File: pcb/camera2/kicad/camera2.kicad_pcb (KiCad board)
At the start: 4 copper layers, 96.5 x 45.7 mm, 56 parts

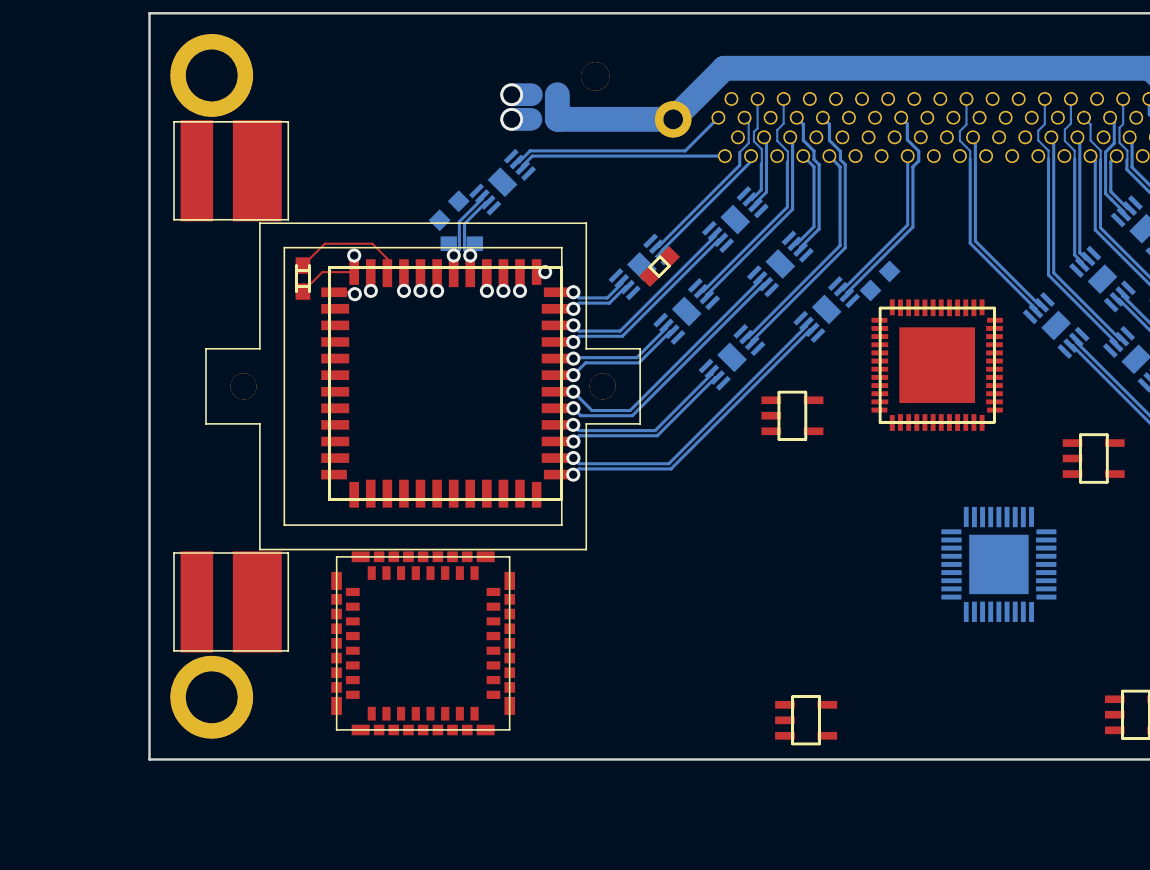
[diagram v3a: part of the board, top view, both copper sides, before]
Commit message: external CPLD pins routed
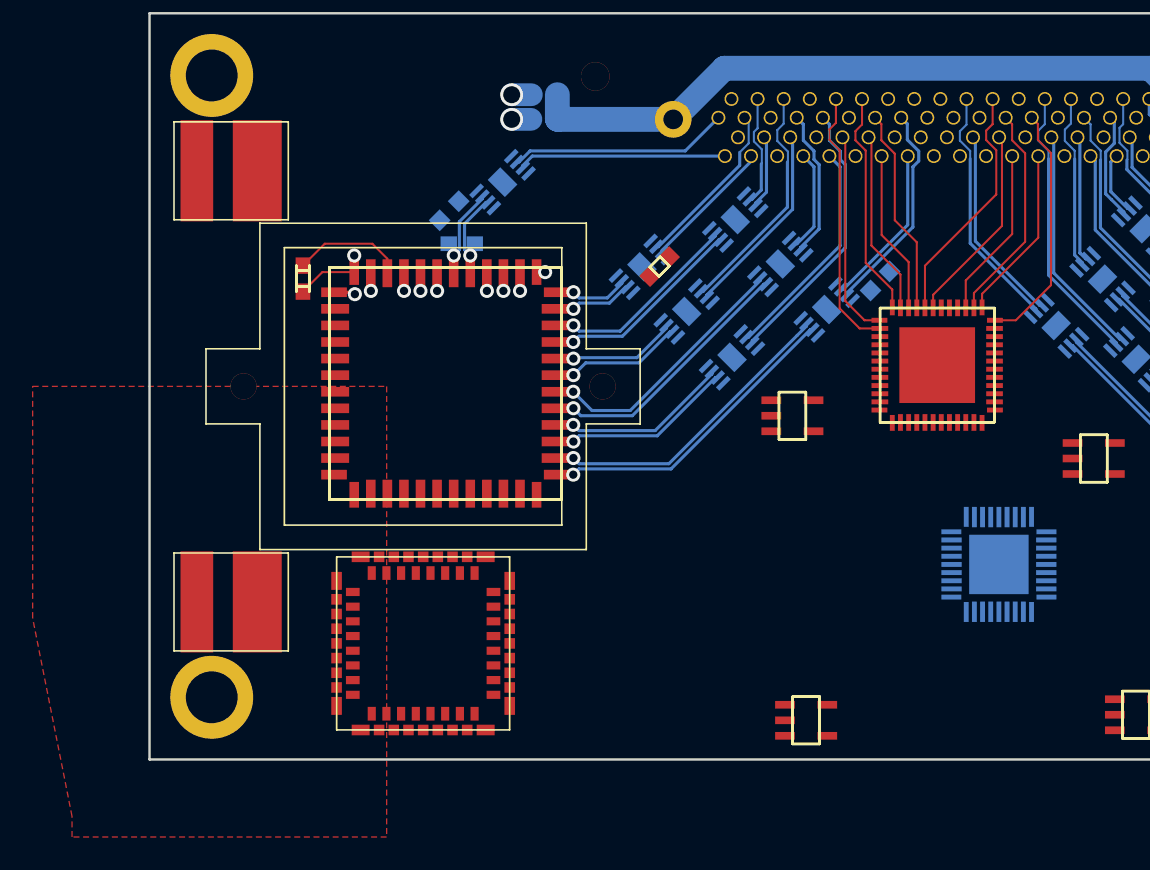
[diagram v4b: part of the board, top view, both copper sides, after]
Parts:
- B1, B10, B11, B15, B16, B17, B18, B19, B2, B20, B3, B4, B5, B6: footprint gen:b84940fdfb16a2d7942b3b406dd98b10c2c2213999c6866e353299b244b8fc6e -> gen:cbfca23ea51b44d0e50a3924c338fdaf501ecf837853ca0935bf710595246917
- C1U1, C2U1: footprint gen:c58747e0684f9d36f894e920eb782c552f159bd2e92cf7dd16541e289be4d654 -> gen:29d36b60264305e3bb3ff8193f908c1e023f0724867315a44096beda3859eb57
- REG0: footprint gen:a8a9fe32768e32ddc75aa8295cef6929db764d9ac77e4627a54db0fef3c1f31a -> gen:ed70987c828567e2e09b177ee862bde5f7a38a9fe78d493e29e57c7e20deaf47
- REG1: footprint gen:0ebfd6ab58889eb03d8f26c7dd1b53306c9215b0059415f86bfdbb9abe3fdde1 -> gen:2bd25f7f1c5714eb7bf2f04a481733791fc5506059f66161b644c94ef96df4e5
- REG2: footprint gen:eb209b2e1d221af71ed48e28bfe0bb8298d616a411442e29f3453ccc73495e89 -> gen:97f27c9ee76a9ddcafed8a13eebe55523c4eda27fc57fcfd9b753b732235d5a3
- REG3: footprint gen:5bda942c242ea2bebc3cf29ef5f6c3ab9ee59d551a6204d93c9eca0998310be8 -> gen:115de365bb93de9cdb0d1863ddce6b36c3ff55cc7ac346e1776ef7a0d0952155
- U1: footprint gen:2f9b442f54b7add4956d34ec651f64beab61546dadc67e38d2c3fc0b09ac9096 -> gen:f8d22c0c24f01065a72fabcbb4d2d21d35812c608890a960801174ad3b2e1a64
- U2: footprint gen:cf96d1af73b58f8f1f3d64f5194d5234fe541250e2558da2cd5d85457dfd18e6 -> gen:230388a9e77c447920cc8d9b60ac5542707622b54124d58dc54acd5e8b04156f
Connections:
- net B10_1 renamed B10_1_NC
- net B10_4 renamed B10_4_NC
- net B10_5 renamed B10_5_NC
- net B11_1 renamed B11_1_NC
- net B11_4 renamed B11_4_NC
- net B11_5 renamed B11_5_NC
- net B15_1 renamed B15_1_NC
- net B15_4 renamed B15_4_NC
- net B15_5 renamed B15_5_NC
- net B16_1 renamed B16_1_NC
- net B16_4 renamed B16_4_NC
- net B16_5 renamed B16_5_NC
- net B17_1 renamed B17_1_NC
- net B17_4 renamed B17_4_NC
- net B17_5 renamed B17_5_NC
- net B18_1 renamed B18_1_NC
- net B18_4 renamed B18_4_NC
- net B18_5 renamed B18_5_NC
- net B19_1 renamed B19_1_NC
- net B19_4 renamed B19_4_NC
- net B19_5 renamed B19_5_NC
- net B1_1 renamed B1_1_NC
- net B1_4 renamed B1_4_NC
- net B1_5 renamed B1_5_NC
- net B20_1 renamed B20_1_NC
- net B20_4 renamed B20_4_NC
- net B20_5 renamed B20_5_NC
- net B2_1 renamed B2_1_NC
- net B2_4 renamed B2_4_NC
- net B2_5 renamed B2_5_NC
- net B3_1 renamed B3_1_NC
- net B3_4 renamed B3_4_NC
- net B3_5 renamed B3_5_NC
- net B4_1 renamed B4_1_NC
- net B4_4 renamed B4_4_NC
- net B4_5 renamed B4_5_NC
- net B5_1 renamed B5_1_NC
- net B5_4 renamed B5_4_NC
- net B5_5 renamed B5_5_NC
- net B6_1 renamed B6_1_NC
- net B6_4 renamed B6_4_NC
- net B6_5 renamed B6_5_NC
- net D0_1 renamed D0_1_C
- net D0_2 renamed D0_2_A
- net D1_1 renamed D1_1_C
- net D1_2 renamed D1_2_A
- net D2_1 renamed D2_1_C
- net D2_2 renamed D2_2_A
- net D3_1 renamed D3_1_C
- net D3_2 renamed D3_2_A
- net REG0_4 renamed REG0_4_NC
- net REG1_4 renamed REG1_4_NC
- net REG2_4 renamed REG2_4_NC
- net REG3_4 renamed REG3_4_NC
- net T1_17 renamed T1_17_NC
- net T1_2 renamed T1_2_GPIO3
- net T1_23 renamed T1_23_PWR_DWN_L
- net T1_24 renamed T1_24_RESET_L
- net T1_26 renamed T1_26_MASTER_CLK
- net T1_28 renamed T1_28_MIPI_CLK_N
- net T1_29 renamed T1_29_MIPI_CLK_P
- net T1_3 renamed T1_3_GPIO2
- net T1_31 renamed T1_31_MIPI_DATA_N
- net T1_32 renamed T1_32_MIPI_DATA_P
- net T1_4 renamed T1_4_GPIO1
- net T1_5 renamed T1_5_GPIO0
- net T2_17 renamed T2_17_NC
- net T2_2 renamed T2_2_GPIO3
- net T2_23 renamed T2_23_PWR_DWN_L
- net T2_24 renamed T2_24_RESET_L
- net T2_26 renamed T2_26_MASTER_CLK
- net T2_28 renamed T2_28_MIPI_CLK_N
- net T2_29 renamed T2_29_MIPI_CLK_P
- net T2_3 renamed T2_3_GPIO2
- net T2_31 renamed T2_31_MIPI_DATA_N
- net T2_32 renamed T2_32_MIPI_DATA_P
- net T2_4 renamed T2_4_GPIO1
- net T2_5 renamed T2_5_GPIO0
- net U1_10 renamed U1_10_PA3
- net U1_11 renamed U1_11_PA4
- net U1_12 renamed U1_12_PA5
- net U1_13 renamed U1_13_PA6
- net U1_14 renamed U1_14_PA7
- net U1_15 renamed U1_15_PB0
- net U1_16 renamed U1_16_PB1
- net U1_17 renamed U1_17_PB2
- net U1_2 renamed U1_2_PD0
- net U1_20 renamed U1_20_PA8
- net U1_21 renamed U1_21_PA9
- net U1_22 renamed U1_22_PA10
- net U1_23 renamed U1_23_PA11
- net U1_24 renamed U1_24_PA12
- net U1_3 renamed U1_3_PD1
- net U1_32 renamed U1_32_PB5
- net U1_33 renamed U1_33_PB6
- net U1_34 renamed U1_34_PB7
- net U1_5 renamed U1_5_VSSA
- net U1_6 renamed U1_6_VDDA
- net U1_7 renamed U1_7_PA0
- net U1_8 renamed U1_8_PA1
- net U1_9 renamed U1_9_PA2
- net U2_10 renamed U2_10_IO1_10
- net U2_11 renamed U2_11_IO1_11
- net U2_12 renamed U2_12_IO1_12
- net U2_13 renamed U2_13_IO1_13
- net U2_14 renamed U2_14_IO1_14
- net U2_15 renamed U2_15_IO1_15
- net U2_17 renamed U2_17_IO1_17
- net U2_18 renamed U2_18_IO1_18
- net U2_20 renamed U2_20_IO1_20
- net U2_24 renamed U2_24_IO1_24
- net U2_25 renamed U2_25_IO1_25
- net U2_26 renamed U2_26_IO1_26
- net U2_27 renamed U2_27_IO1_27
- net U2_28 renamed U2_28_IO1_28
- net U2_30 renamed U2_30_IO1_30
- net U2_32 renamed U2_32_IO2_32
- net U2_33 renamed U2_33_IO2_33
- net U2_34 renamed U2_34_IO2_34
- net U2_35 renamed U2_35_IO2_35
- net U2_4 renamed U2_4_IO2_4
- net U2_5 renamed U2_5_IO2_5
- net U2_6 renamed U2_6_IO1_6
- net U2_7 renamed U2_7_IO1_7
- net U2_8 renamed U2_8_IO1_8
- net U2_9 renamed U2_9_IO1_9
- U2 pad 1: U2_1 -> pair7P
- U2 pad 2: U2_2 -> pair7N
- U2 pad 36: U2_36 -> pair14N
- U2 pad 37: U2_37 -> pair14P
- U2 pad 38: U2_38 -> pair13N
- U2 pad 39: U2_39 -> pair13P
- U2 pad 43: U2_43 -> pair12P
- U2 pad 44: U2_44 -> pair12N
- U2 pad 45: U2_45 -> pair9N
- U2 pad 46: U2_46 -> pair9P
- U2 pad 47: U2_47 -> pair8P
- U2 pad 48: U2_48 -> pair8N
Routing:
- net pair7N: track 0.00 -> 16.2 mm
- net pair14N: track 0.00 -> 15.1 mm
- net pair12N: track 0.00 -> 15.0 mm
- net pair8N: track 0.00 -> 13.9 mm
- net pair13N: track 0.00 -> 13.4 mm
- net pair9N: track 0.00 -> 12.7 mm
- net pair7P: track 0.00 -> 12.7 mm
- net pair12P: track 0.00 -> 12.3 mm
- net pair8P: track 0.00 -> 11.3 mm
- net pair14P: track 0.00 -> 10.7 mm
- net pair13P: track 0.00 -> 10.5 mm
- net pair9P: track 0.00 -> 9.98 mm
- added copper zone on F.Cu, net D1_2_A

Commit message: XXX
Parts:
- B1, B10, B11, B15, B16, B17, B18, B19, B2, B20, B3, B4, B5, B6: footprint gen:cbfca23ea51b44d0e50a3924c338fdaf501ecf837853ca0935bf710595246917 -> gen:3f0d5abe6f072d4a5d6660d5215d8168d11660b29e5e1560198caf100e444ec7
- C1U1, C2U1: footprint gen:29d36b60264305e3bb3ff8193f908c1e023f0724867315a44096beda3859eb57 -> gen:6c7b80def8bd3a6bf34c251afa4212a1888f5eefebf944720aea773b03175eb5
- REG0: footprint gen:ed70987c828567e2e09b177ee862bde5f7a38a9fe78d493e29e57c7e20deaf47 -> gen:c83b3599c72545052e41d59157f57d5e8f7643cc723d0ceb8dfb30e7f518157e
- REG1: footprint gen:2bd25f7f1c5714eb7bf2f04a481733791fc5506059f66161b644c94ef96df4e5 -> gen:61e7f53539b362de3f5caaa35938ff52f28a816c49e3fa7c0c5223f8b8404b80
- REG2: footprint gen:97f27c9ee76a9ddcafed8a13eebe55523c4eda27fc57fcfd9b753b732235d5a3 -> gen:e9a2aba7aa00156e5ec4a59e4d6b66b427f6f11909ae2d572f9b74566f3187db
- REG3: footprint gen:115de365bb93de9cdb0d1863ddce6b36c3ff55cc7ac346e1776ef7a0d0952155 -> gen:b37979a971cec6bf0e63d89cdd2557b488468729de982e385f878d3f3e16fc6a
- U1: footprint gen:f8d22c0c24f01065a72fabcbb4d2d21d35812c608890a960801174ad3b2e1a64 -> gen:f64326a2b4df1a5c4232ac507a0755631b0414d31c50a7c3f952ce896273252c
- turned U2 to 270 degrees
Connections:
- net C1cs_n renamed C1_ss_n
- net C2cs_n renamed C2_ss_n
- REG0 pad 5: vcc1_2 -> vcc1_8
- REG2 pad 5: vcc1_8 -> vcc1_2
- U2 pad 1: pair7P -> pair14N
- U2 pad 10: U2_10_IO1_10 -> pair8P
- U2 pad 11: U2_11_IO1_11 -> pair8N
- U2 pad 12: U2_12_IO1_12 -> pair7P
- U2 pad 13: U2_13_IO1_13 -> pair7N
- U2 pad 2: pair7N -> pair14P
- U2 pad 36: pair14N -> U2_36_IO2_36
- U2 pad 37: pair14P -> U2_37_IO2_37
- U2 pad 38: pair13N -> U2_38_IO2_38
- U2 pad 39: pair13P -> U2_39_IO2_39
- U2 pad 4: U2_4_IO2_4 -> pair13N
- U2 pad 43: pair12P -> U2_43_IO2_43
- U2 pad 44: pair12N -> U2_44_IO2_44
- U2 pad 45: pair9N -> U2_45_IO2_45
- U2 pad 46: pair9P -> U2_46_IO2_46
- U2 pad 47: pair8P -> U2_47_IO2_47
- U2 pad 48: pair8N -> U2_48_IO2_48
- U2 pad 5: U2_5_IO2_5 -> pair13P
- U2 pad 6: U2_6_IO1_6 -> pair12P
- U2 pad 7: U2_7_IO1_7 -> pair12N
- U2 pad 8: U2_8_IO1_8 -> pair9N
- U2 pad 9: U2_9_IO1_9 -> pair9P
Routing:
- net MISO: track 0.00 -> 23.8 mm
- net C1trigger0: track 0.00 -> 21.7 mm
- net C1trigger1: track 0.00 -> 19.2 mm
- net C1trigger2: track 0.00 -> 16.7 mm
- net C1monitor0: track 0.00 -> 15.5 mm
- net C1monitor1: track 0.00 -> 14.4 mm
- net (no net): track 0.00 -> 14.2 mm
- net C1reset_n: track 0.00 -> 13.2 mm
- net MOSI: track 0.00 -> 12.9 mm
- net C1_ss_n: track 0.00 -> 12.0 mm
- net T1_26_MASTER_CLK: track 0.00 -> 8.00 mm
- net T1_23_PWR_DWN_L: track 0.00 -> 6.68 mm
- net SCLK: track 0.00 -> 6.66 mm
- net pair14N: track 15.1 -> 13.7 mm
- net pair7P: track 12.7 -> 11.7 mm

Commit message: before larger cpld
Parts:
- added L0: , gen:14fdd466f7178f17380f48cf89da463f18b4a0e8fcfb609cb3e620722c947cd3, B.Cu at (149.8, 116.5)
- added L1: , gen:14fdd466f7178f17380f48cf89da463f18b4a0e8fcfb609cb3e620722c947cd3, B.Cu at (150.8, 116.5)
- added L2: , gen:14fdd466f7178f17380f48cf89da463f18b4a0e8fcfb609cb3e620722c947cd3, B.Cu at (151.9, 116.5)
- added L3: , gen:14fdd466f7178f17380f48cf89da463f18b4a0e8fcfb609cb3e620722c947cd3, B.Cu at (153.0, 116.5)
- added RT: , gen:57f8f96f6e6b2a00af4539d585b2f3bdc0d73935af5ecd13a4a5208aab3df262, B.Cu at (151.1, 107.4)
- added U3: , gen:80313a3e577ad6f11b72c2abe74f0b6693dabd05551230f1f1f34e41c130c0e0, B.Cu at (151.4, 111.9)
- added U3C: , gen:14fdd466f7178f17380f48cf89da463f18b4a0e8fcfb609cb3e620722c947cd3, B.Cu at (145.8, 113.0)
- B1, B10, B11, B15, B16, B17, B18, B19, B2, B20, B3, B4, B5, B6: footprint gen:3f0d5abe6f072d4a5d6660d5215d8168d11660b29e5e1560198caf100e444ec7 -> gen:3d38d65c100b6aead619492f390645d2b3e8d681eafa555a532e446fd368cdfe
- C1U1, C2U1: footprint gen:6c7b80def8bd3a6bf34c251afa4212a1888f5eefebf944720aea773b03175eb5 -> gen:10664f9dd6177ce506434faab979da9940bc5d6708cf5ab191b3981663e60871
- REG0: footprint gen:c83b3599c72545052e41d59157f57d5e8f7643cc723d0ceb8dfb30e7f518157e -> gen:9307145be34b838094d50d6127d267a01064a34262a858c6cc372ed45fbcf923
- REG1: footprint gen:61e7f53539b362de3f5caaa35938ff52f28a816c49e3fa7c0c5223f8b8404b80 -> gen:3f20292ba4d13303f6409eaa747039e0a582959419ed18ba4e4aba019cd1d96a
- REG2: footprint gen:e9a2aba7aa00156e5ec4a59e4d6b66b427f6f11909ae2d572f9b74566f3187db -> gen:483bd425d8bab395efb60625be80c85a5fefd4678077339d4694436ec1c022e6
- REG3: footprint gen:b37979a971cec6bf0e63d89cdd2557b488468729de982e385f878d3f3e16fc6a -> gen:123d81daf45eb7ed1e1b6a64120b0a1dbdff9846c7f8e55397529a55efe676b0
- U1: footprint gen:f64326a2b4df1a5c4232ac507a0755631b0414d31c50a7c3f952ce896273252c -> gen:e8f52075ef0fec7eeda68900a2821086d1141156e5d1efd66789b578e79d2fd0; moved to F.Cu
- U2: footprint gen:230388a9e77c447920cc8d9b60ac5542707622b54124d58dc54acd5e8b04156f -> gen:256d909fbafaab98513a0740e190710aa9cca955fd39664bcfd9360a469d33f3
- moved U1 27.2 mm to (168.4, 132.8)
- moved B4C 4.06 mm to (156.6, 70.3)
- moved B5C 0.14 mm to (146.5, 69.0)
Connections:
- C1U1 pad 2: MOSI -> C1MOSI
- C1U1 pad 3: MISO -> C1MISO
- C1U1 pad 4: SCLK -> C1SCLK
- C2U1 pad 2: MOSI -> C2MOSI
- C2U1 pad 3: MISO -> C2MISO
- C2U1 pad 4: SCLK -> C2SCLK
- D0 pad 1: D0_1_C -> cat0
- D0 pad 2: D0_2_A -> led0
- D1 pad 1: D1_1_C -> cat1
- D1 pad 2: D1_2_A -> led1
- D2 pad 1: D2_1_C -> cat2
- D2 pad 2: D2_2_A -> led2
- D3 pad 1: D3_1_C -> cat3
- D3 pad 2: D3_2_A -> led3
- REG0 pad 5: vcc1_8 -> vcc1_2
- REG2 pad 5: vcc1_2 -> vcc1_8
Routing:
- net MOSI: track 12.9 -> 3.96 mm
- net C1MOSI: track 0.00 -> 8.91 mm
- net MISO: track 23.8 -> 16.0 mm
- net C1MISO: track 0.00 -> 7.81 mm
- net SCLK: track 6.66 -> 0.00 mm
- net C1SCLK: track 0.00 -> 6.66 mm
- net pair7N: track 16.0 -> 15.4 mm
